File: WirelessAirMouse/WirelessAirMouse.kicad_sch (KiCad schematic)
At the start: 5 parts, among them U1 ESP32-C3-SuperMini, U2 MPU-6050

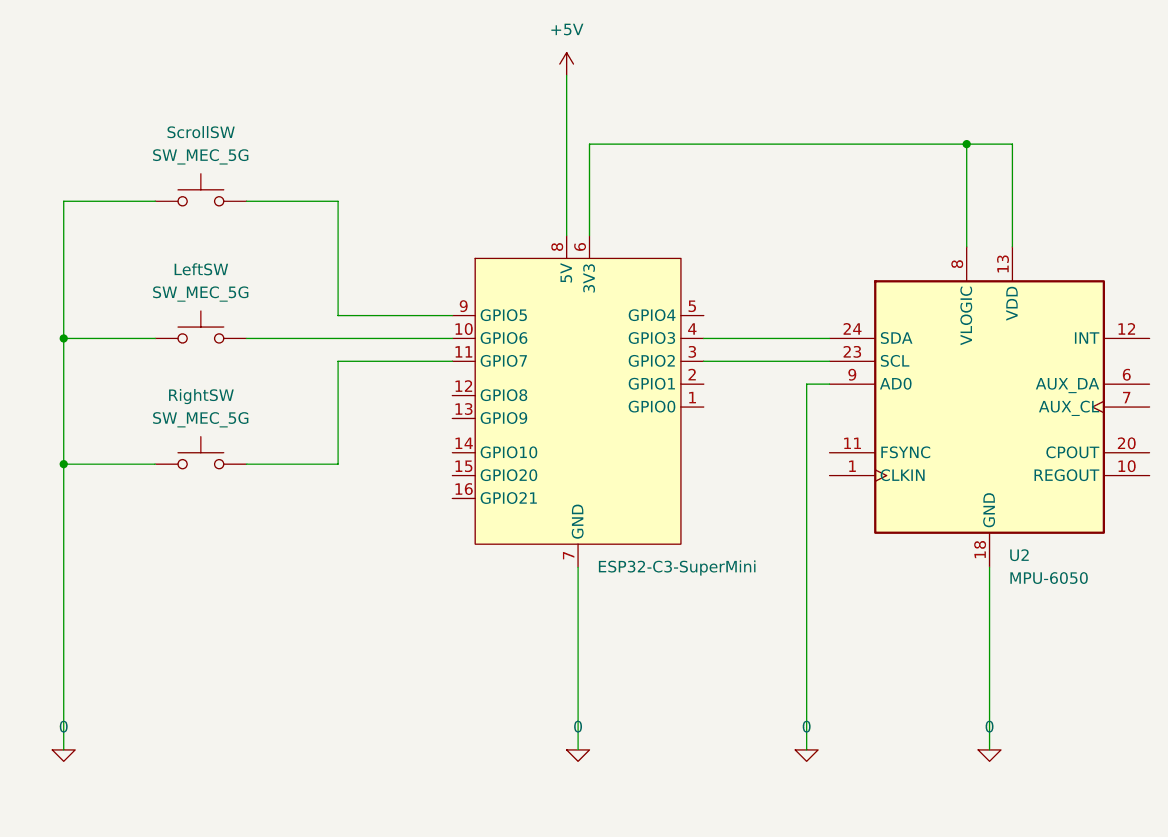
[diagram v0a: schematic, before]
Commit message: docs: update schematic for ESP32-S3 Super Mini and add breadboard photo
- Re-export schematic SVG and 300 DPI PNG from updated KiCad schematic
- Embed breadboard prototype photo into README
- Update KiCad project files and symbol library table
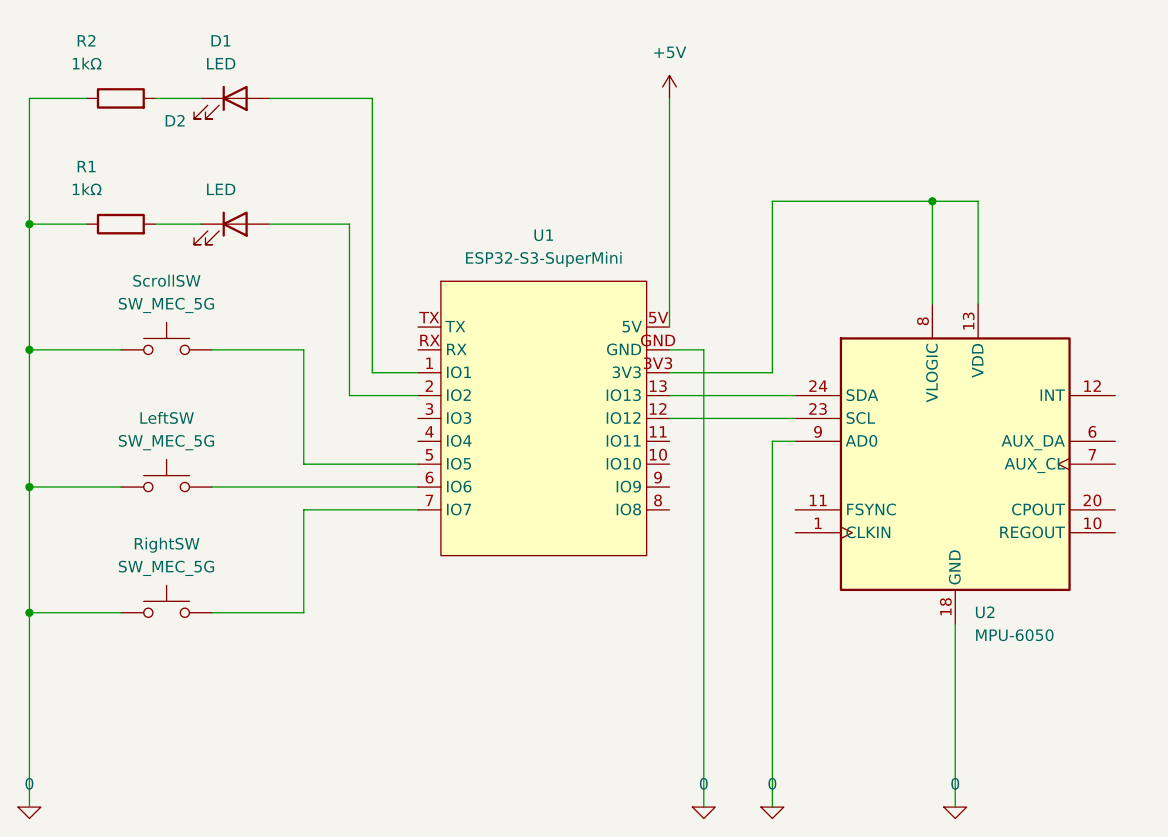
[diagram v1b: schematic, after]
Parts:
- removed U1: ESP32-C3-SuperMini, ESP32-C3-SuperMini:ESP32-C3-SuperMini, symbol ESP32-C3-SuperMini:ESP32-C3-SuperMini
- added D1, D2: LED, symbol Device:LED
- added R1, R2: 1kΩ, symbol Device:R
- added U1: ESP32-S3-SuperMini, ESP32-S3-SuperMini:ESP32-S3-SuperMini, symbol ESP32-S3-SuperMini:ESP32-S3-SuperMini
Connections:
- net +5V: now also U1.5V
- net 0: now also R1.1, R2.1, U1.GND
- net at U2.13 (VDD), U2.8 (VLOGIC): now also U1.3V3
- net at U2.23 (SCL): now also U1.12 (IO12)
- net at U2.24 (SDA): now also U1.13 (IO13)
- net at ScrollSW.3 (B), ScrollSW.4 (B): now also U1.5 (IO5)
- net at LeftSW.3 (B), LeftSW.4 (B): now also U1.6 (IO6)
- net at RightSW.3 (B), RightSW.4 (B): now also U1.7 (IO7)
- new net: D2.1 (K), R1.2
- new net: D1.1 (K), R2.2
- new net: D1.2 (A), U1.1 (IO1)
- new net: D2.2 (A), U1.2 (IO2)
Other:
- moved on the sheet: LeftSW, RightSW, ScrollSW, U2
